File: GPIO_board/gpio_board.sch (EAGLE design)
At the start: 15 parts, among them J1 SWITCHES, J2 LED1, J3 LED2, Q1 IRF520, Q2 IRF520, Q3 IRF520, X1 PCI-E-164SLOT

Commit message: connected a bunch of things to a bunch of things
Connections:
- new net N$29: U$2.32, X1.A40
- new net N$30: U$2.48, X1.A41
- new net N$31: U$2.64, X1.A42
- new net N$32: U$2.80, X1.A43
- new net N$33: U$2.96, X1.A44
- new net N$34: U$2.112, X1.A45
- new net N$35: U$2.128, X1.A46
- new net N$36: U$2.144, X1.A47
- new net N$37: U$2.160, X1.A48
- new net N$38: U$2.176, X1.A49
- new net N$39: U$2.192, X1.A50
- new net N$40: U$2.208, X1.A51
- new net N$41: U$2.224, X1.A52
- new net N$42: U$2.240, X1.A53
- new net N$43: U$2.256, X1.A54
- net N$13: now also U$2.5; no longer U$2.P$5
- net N$14: now also U$2.16; no longer U$2.P$16
- net N$15: now also U$2.15; no longer U$2.P$15
- net N$16: now also U$2.14; no longer U$2.P$14
- net N$17: now also U$2.13; no longer U$2.P$13
- net N$18: now also U$2.12; no longer U$2.P$12
- net N$19: now also U$2.11; no longer U$2.P$11
- net N$20: now also U$2.10; no longer U$2.P$10
- net N$21: now also U$2.9; no longer U$2.P$9
- net N$22: now also U$2.8; no longer U$2.P$8
- net N$23: now also U$2.7; no longer U$2.P$7
- net N$24: now also U$2.6; no longer U$2.P$6
- net N$25: now also U$2.4; no longer U$2.P$4
- net N$26: now also U$2.3; no longer U$2.P$3
- net N$27: now also U$2.2; no longer U$2.P$2
- net N$28: now also U$2.1; no longer U$2.P$1

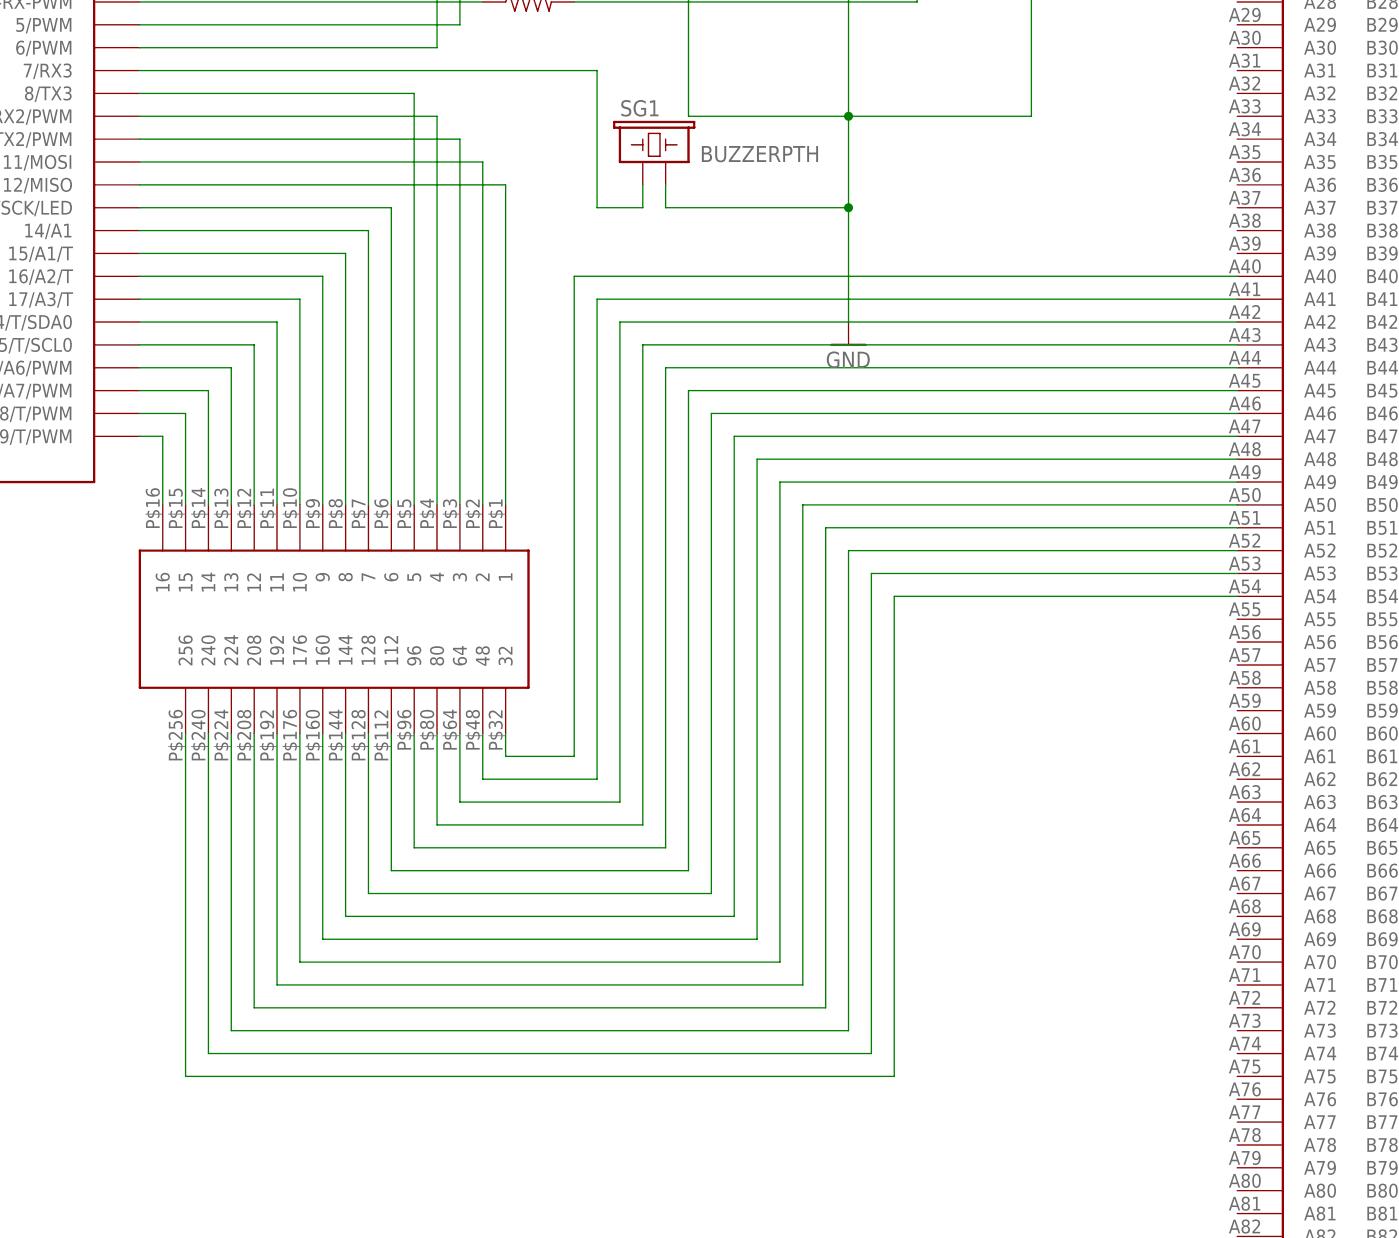
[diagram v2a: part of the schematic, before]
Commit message: re-routed wires so i could stop f***ing getting mixed up on orientation
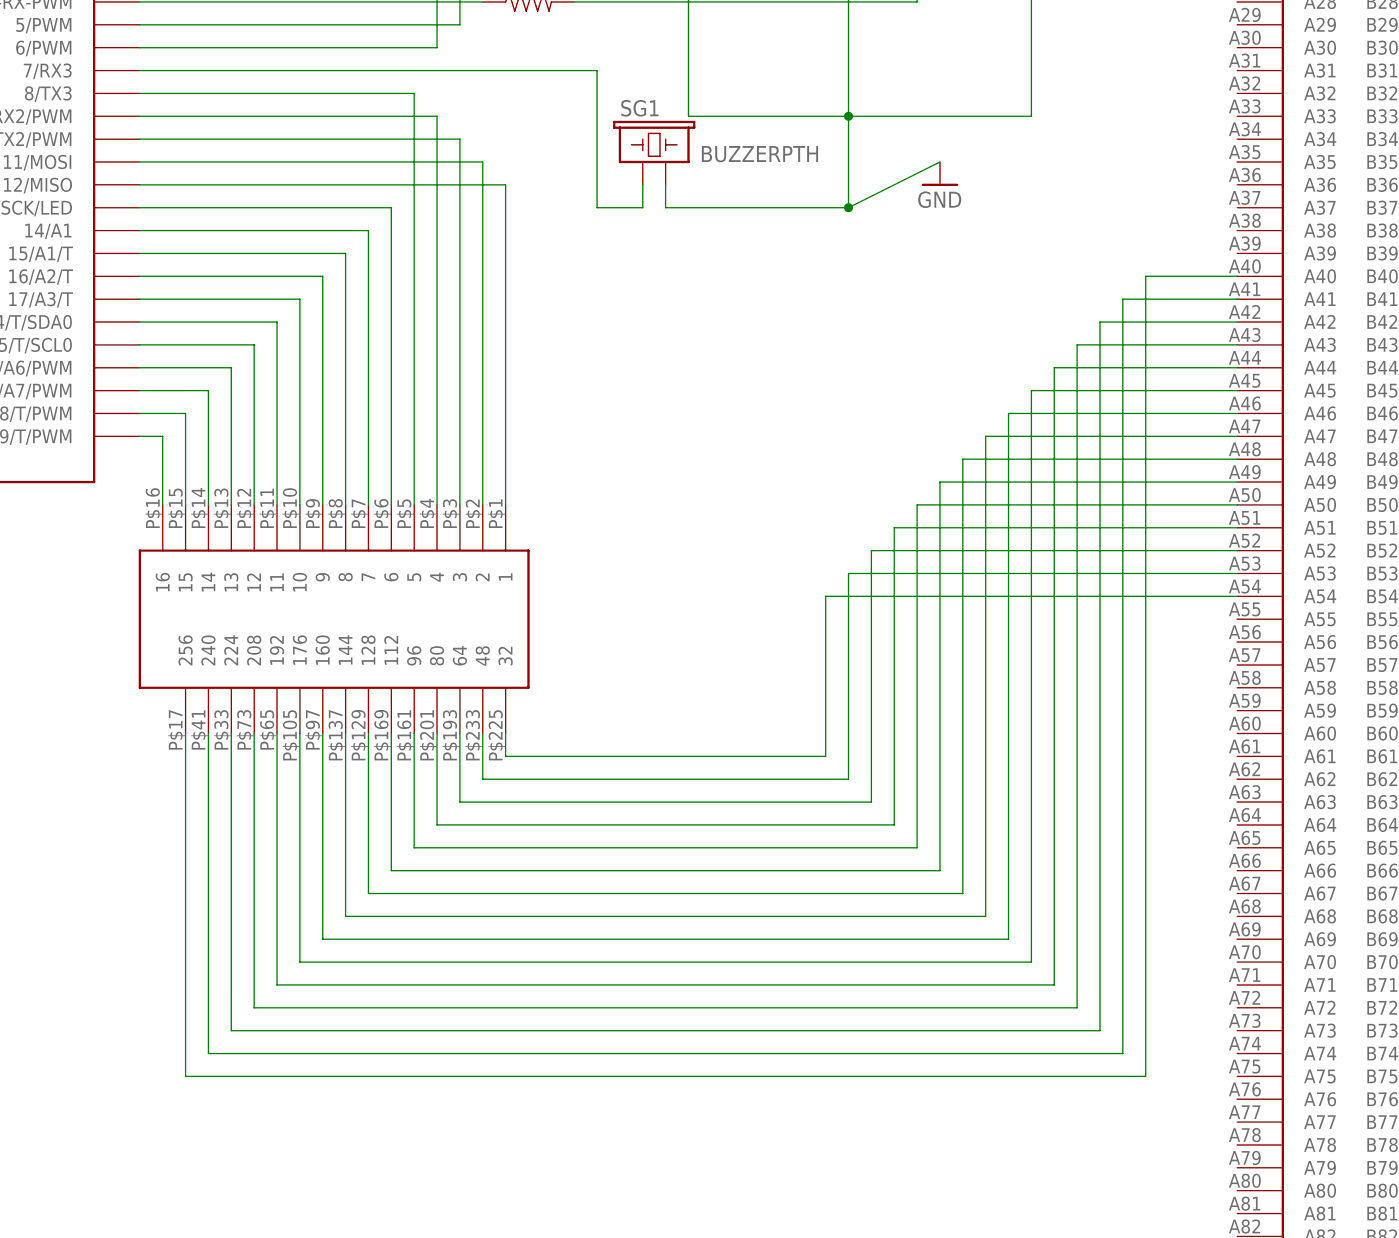
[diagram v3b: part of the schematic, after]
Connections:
- net N$29: now also X1.A54; no longer X1.A40
- net N$30: now also X1.A53; no longer X1.A41
- net N$31: now also X1.A52; no longer X1.A42
- net N$32: now also X1.A51; no longer X1.A43
- net N$33: now also X1.A50; no longer X1.A44
- net N$34: now also X1.A49; no longer X1.A45
- net N$35: now also X1.A48; no longer X1.A46
- net N$37: now also X1.A46; no longer X1.A48
- net N$38: now also X1.A45; no longer X1.A49
- net N$39: now also X1.A44; no longer X1.A50
- net N$40: now also X1.A43; no longer X1.A51
- net N$41: now also X1.A42; no longer X1.A52
- net N$42: now also X1.A41; no longer X1.A53
- net N$43: now also X1.A40; no longer X1.A54

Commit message: fixed traces from PCIe slot to proto_grid
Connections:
- net N$29: now also X1.A68; no longer X1.A54
- net N$30: now also X1.A66; no longer X1.A53
- net N$31: now also X1.A64; no longer X1.A52
- net N$32: now also X1.A62; no longer X1.A51
- net N$33: now also X1.A60; no longer X1.A50
- net N$34: now also X1.A58; no longer X1.A49
- net N$35: now also X1.A56; no longer X1.A48
- net N$36: now also X1.A54; no longer X1.A47
- net N$37: now also X1.A52; no longer X1.A46
- net N$38: now also X1.A50; no longer X1.A45
- net N$39: now also X1.A48; no longer X1.A44
- net N$40: now also X1.A46; no longer X1.A43
- net N$41: now also X1.A44; no longer X1.A42
- net N$42: now also X1.A42; no longer X1.A41
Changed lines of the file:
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@@
 <pinref part="U$2" gate="G$1" pin="32"/>
 <wire x1="160.02" y1="38.1" x2="195.58" y2="38.1" width="0.1524" layer="91"/>
-<wire x1="195.58" y1="38.1" x2="195.58" y2="55.88" width="0.1524" layer="91"/>
-<pinref part="X1" gate="G$1" pin="A54"/>
-<wire x1="195.58" y1="55.88" x2="241.3" y2="55.88" width="0.1524" layer="91"/>
+<pinref part="X1" gate="G$1" pin="A68"/>
+<wire x1="241.3" y1="20.32" x2="238.76" y2="20.32" width="0.1524" layer="91"/>
+<wire x1="238.76" y1="20.32" x2="238.76" y2="-5.08" width="0.1524" layer="91"/>
+<wire x1="238.76" y1="-5.08" x2="195.58" y2="-5.08" width="0.1524" layer="91"/>
+<wire x1="195.58" y1="-5.08" x2="195.58" y2="38.1" width="0.1524" layer="91"/>
 </segment>
 </net>
@@
 <pinref part="U$2" gate="G$1" pin="48"/>
 <wire x1="157.48" y1="35.56" x2="198.12" y2="35.56" width="0.1524" layer="91"/>
-<wire x1="198.12" y1="35.56" x2="198.12" y2="58.42" width="0.1524" layer="91"/>
-<pinref part="X1" gate="G$1" pin="A53"/>
-<wire x1="198.12" y1="58.42" x2="241.3" y2="58.42" width="0.1524" layer="91"/>
+<pinref part="X1" gate="G$1" pin="A66"/>
+<wire x1="241.3" y1="25.4" x2="236.22" y2="25.4" width="0.1524" layer="91"/>
+<wire x1="236.22" y1="25.4" x2="236.22" y2="-2.54" width="0.1524" layer="91"/>
+<wire x1="236.22" y1="-2.54" x2="198.12" y2="-2.54" width="0.1524" layer="91"/>
+<wire x1="198.12" y1="-2.54" x2="198.12" y2="35.56" width="0.1524" layer="91"/>
 </segment>
 </net>
@@
 <pinref part="U$2" gate="G$1" pin="64"/>
 <wire x1="154.94" y1="33.02" x2="200.66" y2="33.02" width="0.1524" layer="91"/>
-<wire x1="200.66" y1="33.02" x2="200.66" y2="60.96" width="0.1524" layer="91"/>
-<pinref part="X1" gate="G$1" pin="A52"/>
-<wire x1="200.66" y1="60.96" x2="241.3" y2="60.96" width="0.1524" layer="91"/>
+<pinref part="X1" gate="G$1" pin="A64"/>
+<wire x1="241.3" y1="30.48" x2="233.68" y2="30.48" width="0.1524" layer="91"/>
+<wire x1="233.68" y1="30.48" x2="233.68" y2="0" width="0.1524" layer="91"/>
+<wire x1="233.68" y1="0" x2="200.66" y2="0" width="0.1524" layer="91"/>
+<wire x1="200.66" y1="0" x2="200.66" y2="33.02" width="0.1524" layer="91"/>
 </segment>
 </net>
@@
 <pinref part="U$2" gate="G$1" pin="80"/>
 <wire x1="152.4" y1="30.48" x2="203.2" y2="30.48" width="0.1524" layer="91"/>
-<wire x1="203.2" y1="30.48" x2="203.2" y2="63.5" width="0.1524" layer="91"/>
-<pinref part="X1" gate="G$1" pin="A51"/>
-<wire x1="203.2" y1="63.5" x2="241.3" y2="63.5" width="0.1524" layer="91"/>
+<pinref part="X1" gate="G$1" pin="A62"/>
+<wire x1="241.3" y1="35.56" x2="203.2" y2="35.56" width="0.1524" layer="91"/>
+<wire x1="203.2" y1="35.56" x2="203.2" y2="30.48" width="0.1524" layer="91"/>
 </segment>
 </net>
@@
 <pinref part="U$2" gate="G$1" pin="96"/>
 <wire x1="149.86" y1="27.94" x2="205.74" y2="27.94" width="0.1524" layer="91"/>
-<wire x1="205.74" y1="27.94" x2="205.74" y2="66.04" width="0.1524" layer="91"/>
-<pinref part="X1" gate="G$1" pin="A50"/>
-<wire x1="205.74" y1="66.04" x2="241.3" y2="66.04" width="0.1524" layer="91"/>
+<pinref part="X1" gate="G$1" pin="A60"/>
+<wire x1="241.3" y1="40.64" x2="205.74" y2="40.64" width="0.1524" layer="91"/>
+<wire x1="205.74" y1="40.64" x2="205.74" y2="27.94" width="0.1524" layer="91"/>
 </segment>
 </net>
@@
 <pinref part="U$2" gate="G$1" pin="112"/>
 <wire x1="147.32" y1="25.4" x2="208.28" y2="25.4" width="0.1524" layer="91"/>
-<wire x1="208.28" y1="25.4" x2="208.28" y2="68.58" width="0.1524" layer="91"/>
-<pinref part="X1" gate="G$1" pin="A49"/>
-<wire x1="208.28" y1="68.58" x2="241.3" y2="68.58" width="0.1524" layer="91"/>
+<pinref part="X1" gate="G$1" pin="A58"/>
+<wire x1="241.3" y1="45.72" x2="208.28" y2="45.72" width="0.1524" layer="91"/>
+<wire x1="208.28" y1="45.72" x2="208.28" y2="25.4" width="0.1524" layer="91"/>
 </segment>
 </net>
@@
 <pinref part="U$2" gate="G$1" pin="128"/>
 <wire x1="144.78" y1="22.86" x2="210.82" y2="22.86" width="0.1524" layer="91"/>
-<wire x1="210.82" y1="22.86" x2="210.82" y2="71.12" width="0.1524" layer="91"/>
-<pinref part="X1" gate="G$1" pin="A48"/>
-<wire x1="210.82" y1="71.12" x2="241.3" y2="71.12" width="0.1524" layer="91"/>
+<pinref part="X1" gate="G$1" pin="A56"/>
+<wire x1="241.3" y1="50.8" x2="210.82" y2="50.8" width="0.1524" layer="91"/>
+<wire x1="210.82" y1="50.8" x2="210.82" y2="22.86" width="0.1524" layer="91"/>
 </segment>
 </net>
@@
 <pinref part="U$2" gate="G$1" pin="144"/>
 <wire x1="142.24" y1="20.32" x2="213.36" y2="20.32" width="0.1524" layer="91"/>
-<wire x1="213.36" y1="20.32" x2="213.36" y2="73.66" width="0.1524" layer="91"/>
-<pinref part="X1" gate="G$1" pin="A47"/>
-<wire x1="213.36" y1="73.66" x2="241.3" y2="73.66" width="0.1524" layer="91"/>
+<pinref part="X1" gate="G$1" pin="A54"/>
+<wire x1="241.3" y1="55.88" x2="213.36" y2="55.88" width="0.1524" layer="91"/>
+<wire x1="213.36" y1="55.88" x2="213.36" y2="20.32" width="0.1524" layer="91"/>
 </segment>
 </net>
@@
 <pinref part="U$2" gate="G$1" pin="160"/>
 <wire x1="139.7" y1="17.78" x2="215.9" y2="17.78" width="0.1524" layer="91"/>
-<wire x1="215.9" y1="17.78" x2="215.9" y2="76.2" width="0.1524" layer="91"/>
-<pinref part="X1" gate="G$1" pin="A46"/>
-<wire x1="215.9" y1="76.2" x2="241.3" y2="76.2" width="0.1524" layer="91"/>
+<pinref part="X1" gate="G$1" pin="A52"/>
+<wire x1="241.3" y1="60.96" x2="215.9" y2="60.96" width="0.1524" layer="91"/>
+<wire x1="215.9" y1="60.96" x2="215.9" y2="17.78" width="0.1524" layer="91"/>
 </segment>
 </net>
@@
 <pinref part="U$2" gate="G$1" pin="176"/>
 <wire x1="137.16" y1="15.24" x2="218.44" y2="15.24" width="0.1524" layer="91"/>
-<wire x1="218.44" y1="15.24" x2="218.44" y2="78.74" width="0.1524" layer="91"/>
-<pinref part="X1" gate="G$1" pin="A45"/>
-<wire x1="218.44" y1="78.74" x2="241.3" y2="78.74" width="0.1524" layer="91"/>
+<pinref part="X1" gate="G$1" pin="A50"/>
+<wire x1="241.3" y1="66.04" x2="218.44" y2="66.04" width="0.1524" layer="91"/>
+<wire x1="218.44" y1="66.04" x2="218.44" y2="15.24" width="0.1524" layer="91"/>
 </segment>
 </net>
@@
 <pinref part="U$2" gate="G$1" pin="192"/>
 <wire x1="134.62" y1="12.7" x2="220.98" y2="12.7" width="0.1524" layer="91"/>
-<wire x1="220.98" y1="12.7" x2="220.98" y2="81.28" width="0.1524" layer="91"/>
-<pinref part="X1" gate="G$1" pin="A44"/>
-<wire x1="220.98" y1="81.28" x2="241.3" y2="81.28" width="0.1524" layer="91"/>
+<pinref part="X1" gate="G$1" pin="A48"/>
+<wire x1="241.3" y1="71.12" x2="220.98" y2="71.12" width="0.1524" layer="91"/>
+<wire x1="220.98" y1="71.12" x2="220.98" y2="12.7" width="0.1524" layer="91"/>
 </segment>
 </net>
@@
 <pinref part="U$2" gate="G$1" pin="208"/>
 <wire x1="132.08" y1="10.16" x2="223.52" y2="10.16" width="0.1524" layer="91"/>
-<wire x1="223.52" y1="10.16" x2="223.52" y2="83.82" width="0.1524" layer="91"/>
-<pinref part="X1" gate="G$1" pin="A43"/>
-<wire x1="223.52" y1="83.82" x2="241.3" y2="83.82" width="0.1524" layer="91"/>
+<pinref part="X1" gate="G$1" pin="A46"/>
+<wire x1="241.3" y1="76.2" x2="223.52" y2="76.2" width="0.1524" layer="91"/>
+<wire x1="223.52" y1="76.2" x2="223.52" y2="10.16" width="0.1524" layer="91"/>
 </segment>
 </net>
@@
 <pinref part="U$2" gate="G$1" pin="224"/>
 <wire x1="129.54" y1="7.62" x2="226.06" y2="7.62" width="0.1524" layer="91"/>
-<wire x1="226.06" y1="7.62" x2="226.06" y2="86.36" width="0.1524" layer="91"/>
-<pinref part="X1" gate="G$1" pin="A42"/>
-<wire x1="226.06" y1="86.36" x2="241.3" y2="86.36" width="0.1524" layer="91"/>
+<pinref part="X1" gate="G$1" pin="A44"/>
+<wire x1="241.3" y1="81.28" x2="226.06" y2="81.28" width="0.1524" layer="91"/>
+<wire x1="226.06" y1="81.28" x2="226.06" y2="7.62" width="0.1524" layer="91"/>
 </segment>
 </net>
@@
 <pinref part="U$2" gate="G$1" pin="240"/>
 <wire x1="127" y1="5.08" x2="228.6" y2="5.08" width="0.1524" layer="91"/>
-<wire x1="228.6" y1="5.08" x2="228.6" y2="88.9" width="0.1524" layer="91"/>
-<pinref part="X1" gate="G$1" pin="A41"/>
-<wire x1="228.6" y1="88.9" x2="241.3" y2="88.9" width="0.1524" layer="91"/>
+<wire x1="228.6" y1="5.08" x2="228.6" y2="86.36" width="0.1524" layer="91"/>
+<pinref part="X1" gate="G$1" pin="A42"/>
+<wire x1="228.6" y1="86.36" x2="241.3" y2="86.36" width="0.1524" layer="91"/>
 </segment>
 </net>
@@
 <wire x1="124.46" y1="2.54" x2="124.46" y2="40.64" width="0.1524" layer="91"/>
 <pinref part="U$2" gate="G$1" pin="256"/>
-<pinref part="X1" gate="G$1" pin="A40"/>
-<wire x1="241.3" y1="91.44" x2="231.14" y2="91.44" width="0.1524" layer="91"/>
 <wire x1="231.14" y1="91.44" x2="231.14" y2="2.54" width="0.1524" layer="91"/>
 <wire x1="231.14" y1="2.54" x2="124.46" y2="2.54" width="0.1524" layer="91"/>
+<pinref part="X1" gate="G$1" pin="A40"/>
+<wire x1="231.14" y1="91.44" x2="241.3" y2="91.44" width="0.1524" layer="91"/>
 </segment>
 </net>

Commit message: added ground pad to proto grid
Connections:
- removed net N$29: U$2.32, X1.A68
- net GND: now also U$2.32, X1.A68
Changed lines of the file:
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@@
 <instance part="R2" gate="G$1" x="162.56" y="127"/>
 <instance part="R3" gate="G$1" x="162.56" y="121.92"/>
-<instance part="GND3" gate="1" x="208.28" y="101.6"/>
+<instance part="GND3" gate="1" x="198.12" y="91.44"/>
 <instance part="R4" gate="G$1" x="129.54" y="170.18" rot="R90"/>
 <instance part="R5" gate="G$1" x="134.62" y="170.18" rot="R90"/>
@@
 <wire x1="218.44" y1="109.22" x2="218.44" y2="129.54" width="0.1524" layer="91"/>
 <pinref part="GND3" gate="1" pin="GND"/>
-<wire x1="208.28" y1="104.14" x2="198.12" y2="99.06" width="0.1524" layer="91"/>
+<wire x1="198.12" y1="93.98" x2="198.12" y2="99.06" width="0.1524" layer="91"/>
 <junction x="198.12" y="109.22"/>
 <pinref part="Q2" gate="G$1" pin="S"/>
@@
 <wire x1="177.8" y1="99.06" x2="198.12" y2="99.06" width="0.1524" layer="91"/>
 <junction x="198.12" y="99.06"/>
+<wire x1="160.02" y1="38.1" x2="160.02" y2="40.64" width="0.1524" layer="91"/>
+<pinref part="U$2" gate="G$1" pin="32"/>
+<wire x1="160.02" y1="38.1" x2="177.8" y2="38.1" width="0.1524" layer="91"/>
+<pinref part="X1" gate="G$1" pin="A68"/>
+<wire x1="177.8" y1="38.1" x2="195.58" y2="38.1" width="0.1524" layer="91"/>
+<wire x1="241.3" y1="20.32" x2="238.76" y2="20.32" width="0.1524" layer="91"/>
+<wire x1="238.76" y1="20.32" x2="238.76" y2="-5.08" width="0.1524" layer="91"/>
+<wire x1="238.76" y1="-5.08" x2="195.58" y2="-5.08" width="0.1524" layer="91"/>
+<wire x1="195.58" y1="-5.08" x2="195.58" y2="38.1" width="0.1524" layer="91"/>
+<wire x1="177.8" y1="38.1" x2="177.8" y2="99.06" width="0.1524" layer="91"/>
+<junction x="177.8" y="38.1"/>
+<junction x="177.8" y="99.06"/>
 </segment>
 <segment>
@@
 </segment>
 </net>
-<net name="N$29" class="0">
-<segment>
-<wire x1="160.02" y1="38.1" x2="160.02" y2="40.64" width="0.1524" layer="91"/>
-<pinref part="U$2" gate="G$1" pin="32"/>
-<wire x1="160.02" y1="38.1" x2="195.58" y2="38.1" width="0.1524" layer="91"/>
-<pinref part="X1" gate="G$1" pin="A68"/>
-<wire x1="241.3" y1="20.32" x2="238.76" y2="20.32" width="0.1524" layer="91"/>
-<wire x1="238.76" y1="20.32" x2="238.76" y2="-5.08" width="0.1524" layer="91"/>
-<wire x1="238.76" y1="-5.08" x2="195.58" y2="-5.08" width="0.1524" layer="91"/>
-<wire x1="195.58" y1="-5.08" x2="195.58" y2="38.1" width="0.1524" layer="91"/>
-</segment>
-</net>
 <net name="N$30" class="0">
 <segment>
@@
 </segment>
 </net>
-<net name="N$43" class="0">
+<net name="N$43" class="1">
 <segment>
 <wire x1="124.46" y1="2.54" x2="124.46" y2="40.64" width="0.1524" layer="91"/>
